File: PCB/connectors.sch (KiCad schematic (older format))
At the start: 8 parts

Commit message: Changed PCB.
- Added MOSFET, connectors sheet
- Changed MCU and power sheet
- Reorganised sheets
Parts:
- removed J?: 62201021121, Connector_PinHeader_1.27mm:PinHeader_2x10_P1.27mm_Vertical, symbol Connector_Generic:Conn_02x10_Odd_Even
- removed J?: Conn_01x06, symbol Connector_Generic:Conn_01x06
- removed TP?: GND_PWR_IN, symbol Connector_Specialized:Test_Point
- removed TP?: VDD_PWR_IN, symbol Connector_Specialized:Test_Point
- removed TP?: GND_BED_IN, symbol Connector_Specialized:Test_Point
- removed TP?: VDD_BED_IN, symbol Connector_Specialized:Test_Point
- removed TP?: BED-, symbol Connector_Specialized:Test_Point
- removed TP?: BED+, symbol Connector_Specialized:Test_Point
- added C? (x8): 100nF, Capacitor_SMD:C_0603_1608Metric, symbol Device:C
- added C? (x3): C, symbol Device:C
- added D? (x6): BAT54GWJ, symbol Device:D_Schottky
- added J?: USB_B, symbol Connector_Specialized:USB_B
- added J? (x3): Conn_02x05_Odd_Even, Connector_PinHeader_2.54mm:PinHeader_2x05_P2.54mm_Vertical, symbol Connector_Generic:Conn_02x05_Odd_Even
- added J? (x3): 70543-0001, Connector_PinHeader_2.54mm:PinHeader_1x02_P2.54mm_Vertical, symbol Connector_Generic:Conn_01x02
- added J? (x6): 70543-0002, Connector_PinHeader_2.54mm:PinHeader_1x03_P2.54mm_Vertical, symbol Connector_Generic:Conn_01x03
- added J?: 62201021121, Connector_PinHeader_1.27mm:PinHeader_2x05_P1.27mm_Vertical, symbol Connector_Generic:Conn_02x05_Odd_Even
- added MK? (x4): Mounting_Hole_PAD, MountingHole:MountingHole_5.3mm_M5_ISO14580_Pad, symbol Mechanical:Mounting_Hole_PAD
- added R? (x4): 10k, Resistor_SMD:R_0603_1608Metric, symbol Device:R
- added R? (x6): 2k37, symbol Device:R
- added R? (x3): 4.7k, 4.7k, symbol Device:R
- added TP?: THERM_1, symbol Connector_Specialized:Test_Point
- added TP?: THERM_2, symbol Connector_Specialized:Test_Point
- added TP?: THERM_3, symbol Connector_Specialized:Test_Point
- added U? (x4): TXB0108PWR, Package_SO:TSSOP-20_4.4x6.5mm_P0.65mm, symbol Logic_LevelTranslator:TXB0108DQSR
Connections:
- net labels added: BTN_EN1, BTN_EN2, BTN_ENC, DD+, DD-, EXT_D1, EXT_D2, EXT_D3, GNDPWR, GNDS, KILL_PIN, LCD_BEEPER, LCD_D4, LCD_D5, LCD_D6, LCD_D7, LCD_EN, LCD_RD, LCD_RS, MCU_BTN_EN1, MCU_BTN_EN2, MCU_BTN_ENC, MCU_EXT_D1, MCU_EXT_D2, MCU_EXT_D3, MCU_KILL_PIN, MCU_LCD_BEEPER, MCU_LCD_D4, MCU_LCD_D5, MCU_LCD_D6, MCU_LCD_D7, MCU_LCD_EN, MCU_LCD_RD, MCU_MISO, MCU_MOSI, MCU_SCK, MCU_SD_CARD_DET, MCU_SSM1, MCU_SSM2, MCU_SSM3, MCU_SSM4, MCU_SSSD, MCU_X_MAX, MCU_X_MIN, MCU_Y_MAX, MCU_Y_MIN, MCU_Z_MAX, MCU_Z_MIN, MISO, MOSI, SCK, SCL, SDA, SD_CARD_DET, SSM1, SSM2, SSM3, SSM4, SSSD, SWCLK, SWDIO, THERM_1, THERM_2, THERM_3, VBUS, VDD3V3, VDD5V, X_MAX, X_MIN, Y_MAX, Y_MIN, Z_MAX, Z_MIN, nRESET
- net labels removed: GND_BED_OUT, VDD_BED_IN, VDD_BED_OUT, VDD_PWR_IN
- wire segments 28 -> 85
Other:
- note added: "ESD protected by USB isolator"
- note added: "ESD protected by level shifter"
- note added: "EXT-LCD"
- note added: "EXT-SD"
- note added: "EXT-SPI-L2C"
- note added: "Endstops"
- note added: "Level Shifter"
- note added: "SWD"
- note added: "Thermistors"
- note added: "USB"
- note removed: "JTAG"

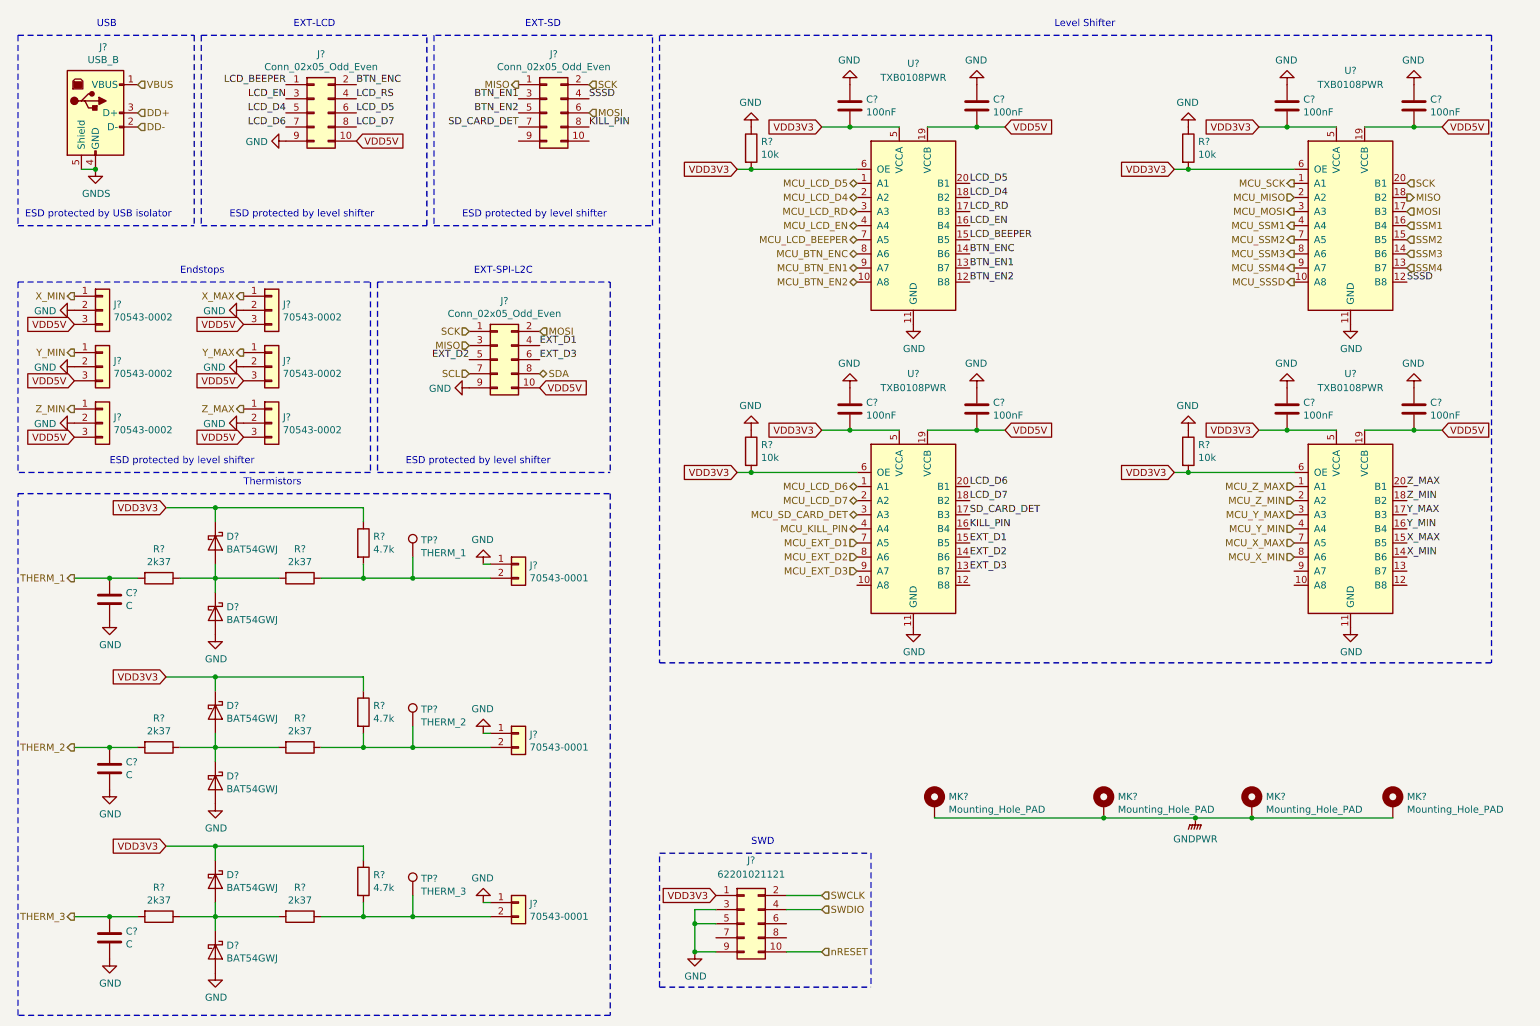
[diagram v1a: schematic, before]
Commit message: Changed some sheets and added LICENCE.
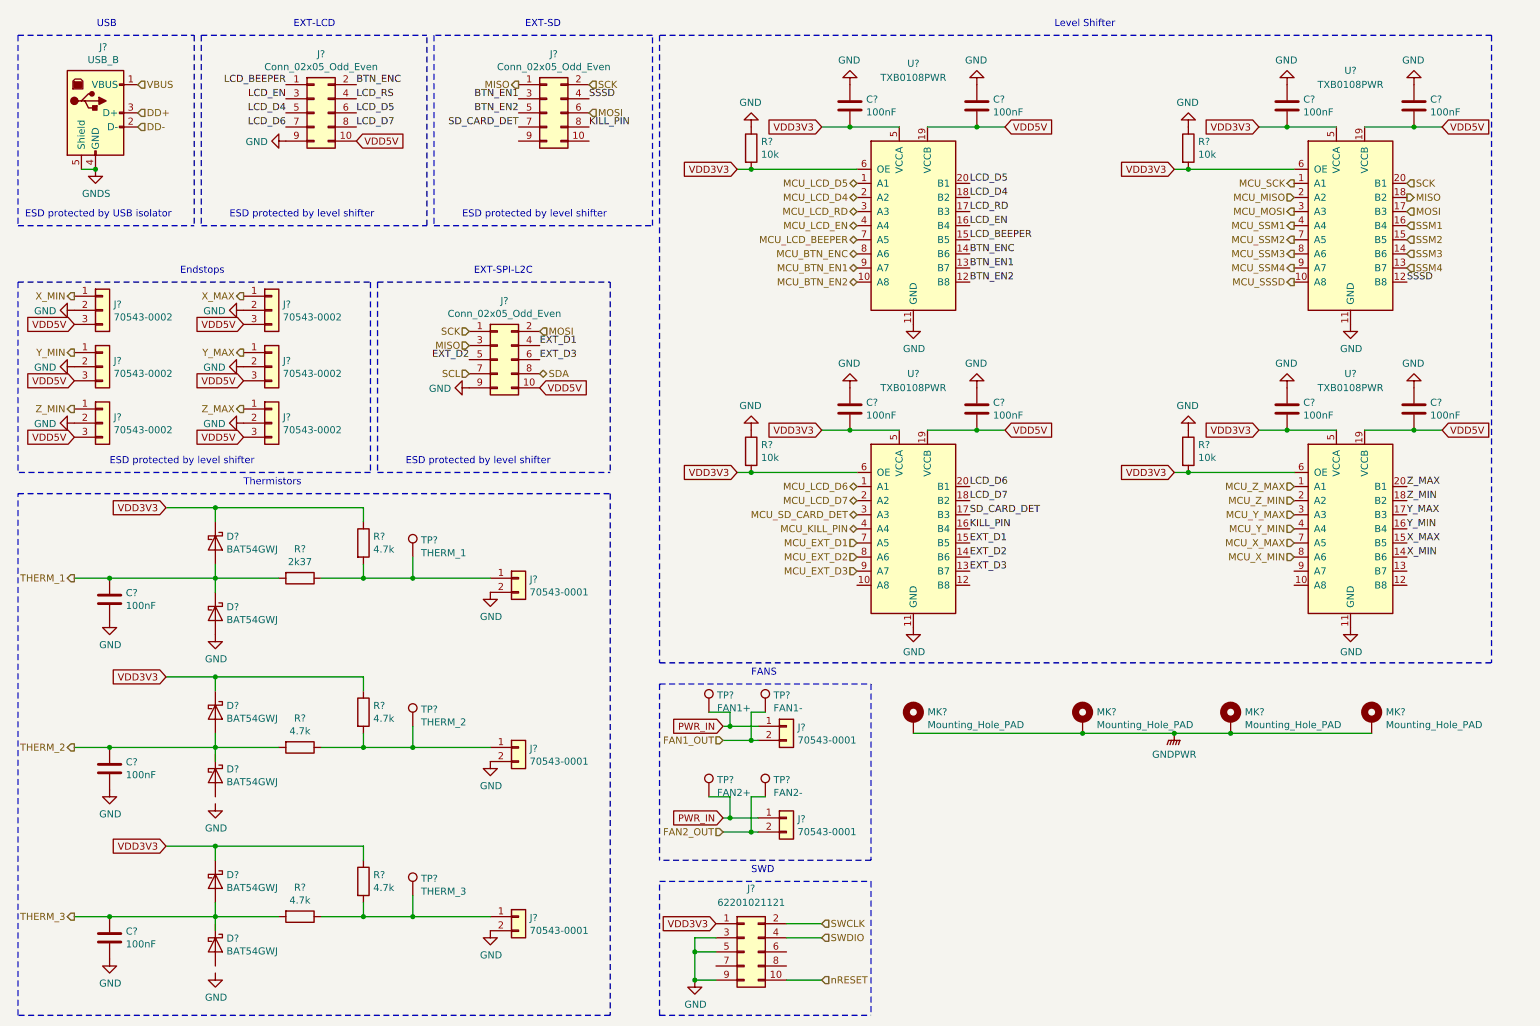
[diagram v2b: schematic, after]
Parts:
- removed D? (x5): BAT54GWJ, symbol Device:D_Schottky
- removed R? (x3): 2k37, symbol Device:R
- added D? (x5): BAT54GWJ, Diode_SMD:D_SOD-123, symbol Device:D_Schottky
- added J? (x2): 70543-0001, Connector_PinHeader_2.54mm:PinHeader_1x02_P2.54mm_Vertical, symbol Connector_Generic:Conn_01x02
- added TP?: FAN1+, TestPoint:TestPoint_Pad_D1.0mm, symbol Connector_Specialized:Test_Point
- added TP?: FAN2+, TestPoint:TestPoint_Pad_D1.0mm, symbol Connector_Specialized:Test_Point
- added TP?: FAN2-, TestPoint:TestPoint_Pad_D1.0mm, symbol Connector_Specialized:Test_Point
- added TP?: FAN1-, TestPoint:TestPoint_Pad_D1.0mm, symbol Connector_Specialized:Test_Point
- C? (x3): value C -> 100nF
- D?: footprint (none) -> Diode_SMD:D_SOD-123
- R?: footprint (none) -> Resistor_SMD:R_0603_1608Metric
- R? (x3): footprint 4.7k -> Resistor_SMD:R_0603_1608Metric
- R? (x2): value 2k37 -> 4.7k; footprint (none) -> Resistor_SMD:R_0603_1608Metric
- TP? (x3): footprint (none) -> TestPoint:TestPoint_Pad_D1.0mm
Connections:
- net GND: now also J?.2 (Pin_2), J?.2 (Pin_2), J?.2 (Pin_2), D?.2 (A); no longer J?.1 (Pin_1), J?.1 (Pin_1), J?.1 (Pin_1)
- net THERM_1: now also D?.2 (A), R?.2, D?.1 (K)
- net THERM_2: now also R?.2, D?.2 (A)
- net THERM_3: now also R?.2, D?.2 (A)
- net VDD3V3: now also D?.1 (K), D?.1 (K)
- net at R?.1, R?.2, TP?.1: now also J?.1 (Pin_1); no longer J?.2 (Pin_2) (x3)
- new net FAN1_OUT: J?.2 (Pin_2), TP?.1
- new net FAN2_OUT: J?.2 (Pin_2), TP?.1
- new net PWR_IN: J?.1 (Pin_1), J?.1 (Pin_1), TP?.1, TP?.1
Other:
- note added: "FANS"
- moved on the sheet: J?, MK?

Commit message: Finished first draft of the schematics.
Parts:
- removed MK? (x4): Mounting_Hole_PAD, MountingHole:MountingHole_5.3mm_M5_ISO14580_Pad, symbol Mechanical:Mounting_Hole_PAD
- removed TP?: FAN1-, TestPoint:TestPoint_Pad_D1.0mm, symbol Connector_Specialized:Test_Point
- added TP?: FAN1-, TestPoint:TestPoint_Pad_D1.0mm, symbol Connector_Specialized:Test_Point
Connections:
- net FAN1_OUT: now also TP?.1
- net X_MAX: now also J?.1 (Pin_1); no longer J?.1 (Pin_1)
- net X_MIN: now also J?.1 (Pin_1); no longer J?.1 (Pin_1)
- net Y_MAX: now also J?.1 (Pin_1); no longer J?.1 (Pin_1)
- net Y_MIN: now also J?.1 (Pin_1); no longer J?.1 (Pin_1)
- net Z_MAX: now also J?.1 (Pin_1); no longer J?.1 (Pin_1)
- net Z_MIN: now also J?.1 (Pin_1); no longer J?.1 (Pin_1)
- net MCU_SSM1 renamed MCU_SSX
- net MCU_SSM2 renamed MCU_SSY
- net MCU_SSM3 renamed MCU_SSZ
- net MCU_SSM4 renamed MCU_SSE
- net SSM1 renamed SSX
- net SSM2 renamed SSY
- net SSM3 renamed SSZ
- net SSM4 renamed SSE
- no-connect marks 0 -> 11
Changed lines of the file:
@@
 $Descr A4 11693 8268
 encoding utf-8
-Sheet 4 5
+Sheet 4 9
 Title "Connectors"
 Date ""
@@
 Text Notes 1750 2450 0    50   ~ 0
 Endstops
-Text HLabel 2200 2600 0    50   Output ~ 0
-X_MAX
-Text HLabel 1000 2600 0    50   Output ~ 0
-X_MIN
 $Comp
 L power:GND #PWR?
@@
 	1    0    0    -1
 $EndComp
-Text HLabel 2200 3000 0    50   Output ~ 0
-Y_MAX
-Text HLabel 1000 3000 0    50   Output ~ 0
-Y_MIN
 $Comp
 L power:GND #PWR?
@@
 	1    0    0    -1
 $EndComp
-Text HLabel 2200 3400 0    50   Output ~ 0
-Z_MAX
-Text HLabel 1000 3400 0    50   Output ~ 0
-Z_MIN
 $Comp
 L power:GND #PWR?
@@
 MCU_MOSI
 Text HLabel 9650 2100 0    50   Output ~ 0
-MCU_SSM1
+MCU_SSX
 Text HLabel 9650 2200 0    50   Output ~ 0
-MCU_SSM2
+MCU_SSY
 Text HLabel 9650 2300 0    50   Output ~ 0
-MCU_SSM3
+MCU_SSZ
 Text HLabel 9650 2400 0    50   Output ~ 0
-MCU_SSM4
+MCU_SSE
 Text HLabel 9650 2500 0    50   Output ~ 0
 MCU_SSSD
@@
 SCK
 Text HLabel 10450 2100 2    50   Input ~ 0
-SSM1
+SSX
 Text HLabel 10450 2200 2    50   Input ~ 0
-SSM2
+SSY
 Text HLabel 10450 2300 2    50   Input ~ 0
-SSM3
+SSZ
 Text HLabel 10450 2400 2    50   Input ~ 0
-SSM4
+SSE
 Text Label 10450 2500 0    50   ~ 0
 SSSD
@@
 Text HLabel 4150 1100 0    50   Output ~ 0
 MISO
-$Comp
-L Mechanical:Mounting_Hole_PAD MK?
-U 1 1 5B1F12A4
-P 6950 5600
-F 0 "MK?" H 7050 5651 50  0000 L CNN
-F 1 "Mounting_Hole_PAD" H 7050 5560 50  0000 L CNN
-F 2 "MountingHole:MountingHole_5.3mm_M5_ISO14580_Pad" H 6950 5600 50  0001 C CNN
-F 3 "" H 6950 5600 50  0001 C CNN
-	1    6950 5600
-	1    0    0    -1
-$EndComp
-$Comp
-L Mechanical:Mounting_Hole_PAD MK?
-U 1 1 5B1F12AB
-P 8150 5600
-F 0 "MK?" H 8250 5651 50  0000 L CNN
-F 1 "Mounting_Hole_PAD" H 8250 5560 50  0000 L CNN
-F 2 "MountingHole:MountingHole_5.3mm_M5_ISO14580_Pad" H 8150 5600 50  0001 C CNN
-F 3 "" H 8150 5600 50  0001 C CNN
-	1    8150 5600
-	1    0    0    -1
-$EndComp
-$Comp
-L Mechanical:Mounting_Hole_PAD MK?
-U 1 1 5B1F12B2
-P 9200 5600
-F 0 "MK?" H 9300 5651 50  0000 L CNN
-F 1 "Mounting_Hole_PAD" H 9300 5560 50  0000 L CNN
-F 2 "MountingHole:MountingHole_5.3mm_M5_ISO14580_Pad" H 9200 5600 50  0001 C CNN
-F 3 "" H 9200 5600 50  0001 C CNN
-	1    9200 5600
-	1    0    0    -1
-$EndComp
-$Comp
-L Mechanical:Mounting_Hole_PAD MK?
-U 1 1 5B1F12B9
-P 10200 5600
-F 0 "MK?" H 10300 5651 50  0000 L CNN
-F 1 "Mounting_Hole_PAD" H 10300 5560 50  0000 L CNN
-F 2 "MountingHole:MountingHole_5.3mm_M5_ISO14580_Pad" H 10200 5600 50  0001 C CNN
-F 3 "" H 10200 5600 50  0001 C CNN
-	1    10200 5600
-	1    0    0    -1
-$EndComp
-$Comp
-L power:GNDPWR #PWR?
-U 1 1 5B1F12C0
-P 8800 5700
-F 0 "#PWR?" H 8800 5500 50  0001 C CNN
-F 1 "GNDPWR" H 8800 5550 50  0000 C CNN
-F 2 "" H 8800 5650 50  0001 C CNN
-F 3 "" H 8800 5650 50  0001 C CNN
-	1    8800 5700
-	1    0    0    -1
-$EndComp
-Wire Wire Line
-	10200 5700 9200 5700
-Connection ~ 8150 5700
-Wire Wire Line
-	8150 5700 6950 5700
-Connection ~ 8800 5700
-Wire Wire Line
-	8800 5700 8150 5700
-Connection ~ 9200 5700
-Wire Wire Line
-	9200 5700 8800 5700
 Wire Wire Line
 	1250 4600 2000 4600
@@
 	1    0    0    -1
 $EndComp
+Wire Wire Line
+	5650 5650 5650 5550
+Wire Wire Line
+	5650 5550 5500 5550
+Connection ~ 5650 5650
+Wire Wire Line
+	5650 5650 5850 5650
+Wire Wire Line
+	5900 5550 5800 5550
+Wire Wire Line
+	5800 5550 5800 5750
+Connection ~ 5800 5750
+Wire Wire Line
+	5800 5750 5850 5750
+Wire Wire Line
+	5500 6150 5650 6150
+Wire Wire Line
+	5650 6150 5650 6300
+Connection ~ 5650 6300
+Wire Wire Line
+	5650 6300 5850 6300
+Wire Wire Line
+	5900 6150 5800 6150
+Wire Wire Line
+	5800 6150 5800 6400
+Connection ~ 5800 6400
+Wire Wire Line
+	5800 6400 5850 6400
+Wire Notes Line
+	6650 5350 6650 6600
+Wire Notes Line
+	5150 5350 5150 6600
 $Comp
 L Connector_Specialized:Test_Point TP?
-U 1 1 5B0144BF
+U 1 1 5B068C7B
 P 5900 5550
 F 0 "TP?" H 5958 5670 50  0000 L CNN
@@
 	1    0    0    -1
 $EndComp
-Wire Wire Line
-	5650 5650 5650 5550
-Wire Wire Line
-	5650 5550 5500 5550
-Connection ~ 5650 5650
-Wire Wire Line
-	5650 5650 5850 5650
-Wire Wire Line
-	5900 5550 5800 5550
-Wire Wire Line
-	5800 5550 5800 5750
-Connection ~ 5800 5750
-Wire Wire Line
-	5800 5750 5850 5750
-Wire Wire Line
-	5500 6150 5650 6150
-Wire Wire Line
-	5650 6150 5650 6300
-Connection ~ 5650 6300
-Wire Wire Line
-	5650 6300 5850 6300
-Wire Wire Line
-	5900 6150 5800 6150
-Wire Wire Line
-	5800 6150 5800 6400
-Connection ~ 5800 6400
-Wire Wire Line
-	5800 6400 5850 6400
-Wire Notes Line
-	6650 5350 6650 6600
-Wire Notes Line
-	5150 5350 5150 6600
+NoConn ~ 4650 1500
+NoConn ~ 4150 1500
+NoConn ~ 10450 4550
+NoConn ~ 10450 4650
+NoConn ~ 9650 4650
+NoConn ~ 9650 4550
+NoConn ~ 7350 4650
+NoConn ~ 6550 4650
+NoConn ~ 5550 7350
+NoConn ~ 6050 7350
+NoConn ~ 6050 7250
+Text Label 1000 2600 2    50   ~ 0
+X_MAX
+Text Label 1000 3000 2    50   ~ 0
+Y_MAX
+Text Label 1000 3400 2    50   ~ 0
+Z_MAX
+Text Label 2200 2600 2    50   ~ 0
+X_MIN
+Text Label 2200 3000 2    50   ~ 0
+Y_MIN
+Text Label 2200 3400 2    50   ~ 0
+Z_MIN
 $EndSCHEMATC
